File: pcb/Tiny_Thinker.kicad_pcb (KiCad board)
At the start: 4 copper layers, 65 x 63.1 mm, 42 parts, among them J2 PERIPHERALS, J3 ADC_TIM, J8 USB_C_Receptacle_USB2.0_16P, SW1 SW_Push, SW2 SW_SPDT, U1 STM32F446RET6, U2 AMS1117-3.3, Y1 16MHz

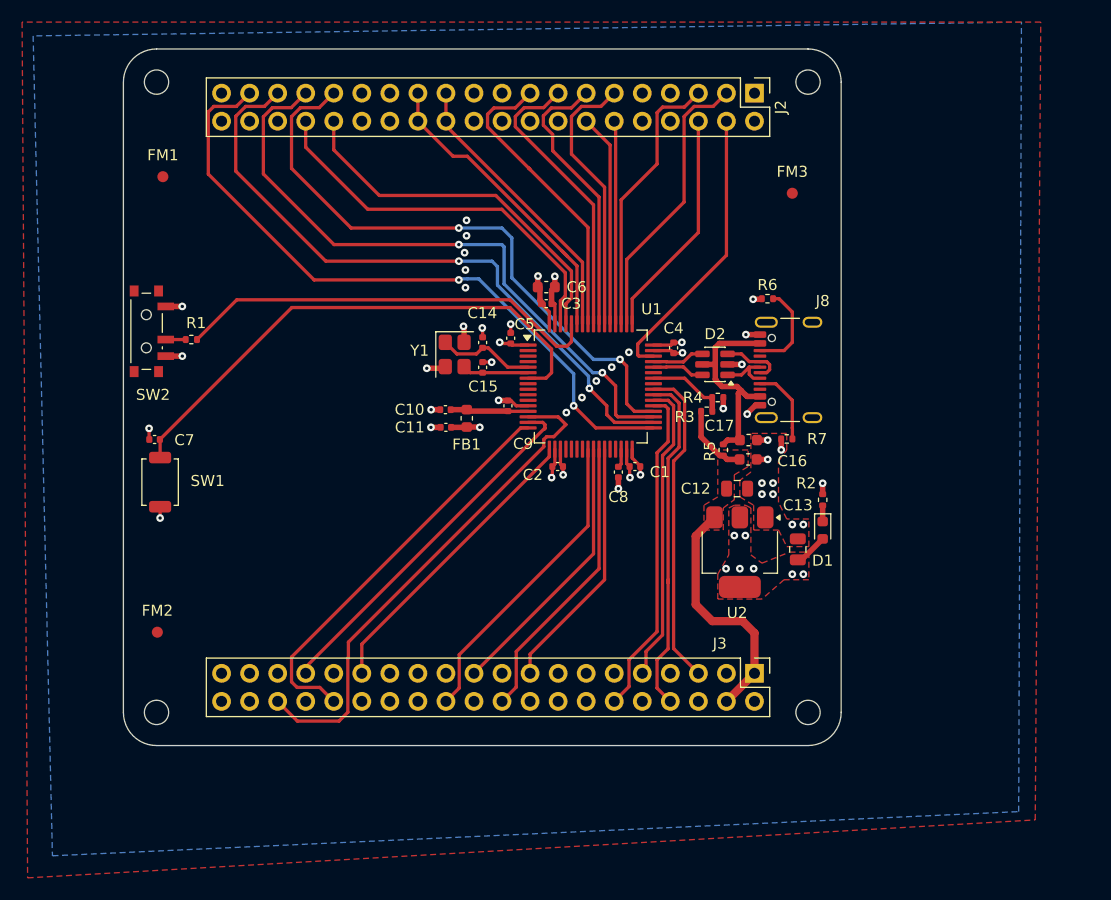
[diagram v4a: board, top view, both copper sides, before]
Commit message: finished adding vias to header pins (not stitching)
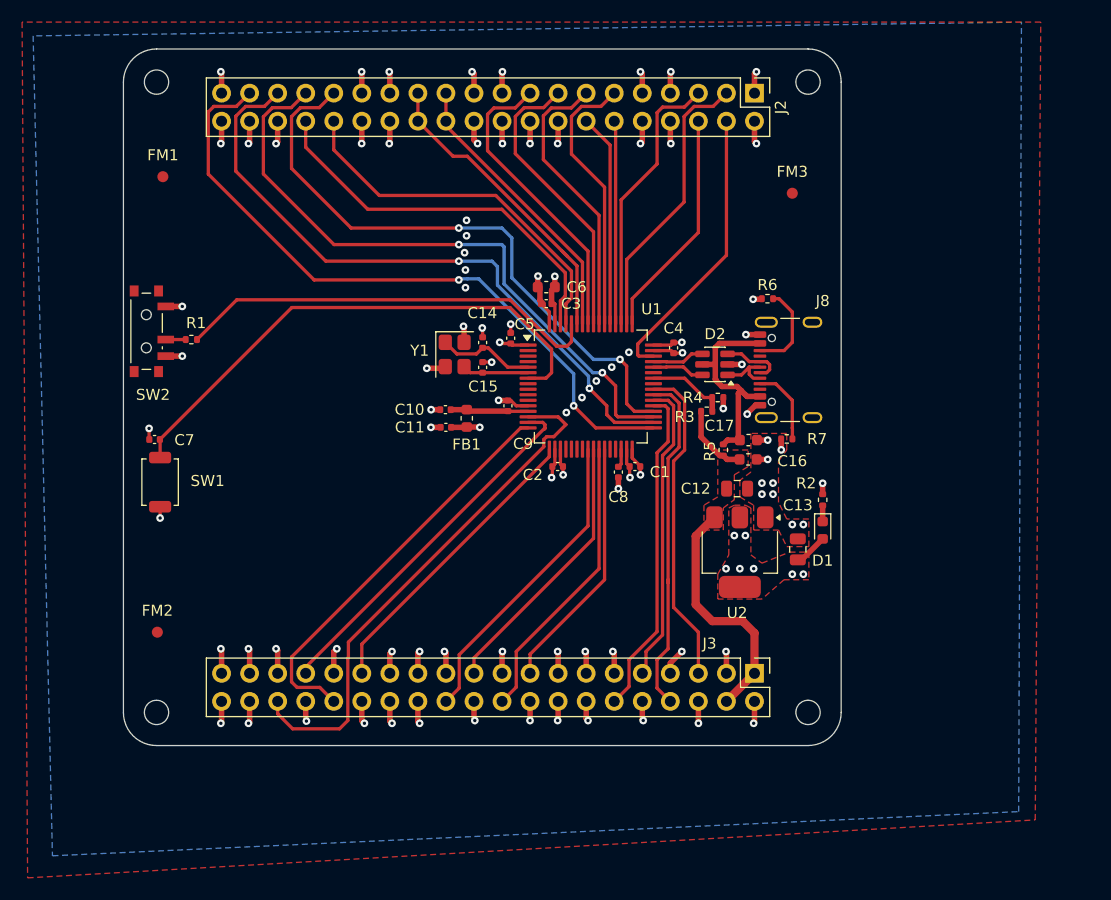
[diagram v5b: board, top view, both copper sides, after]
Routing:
- net GND: track 37.3 -> 97.9 mm, vias 41 -> 71
- net +3.3V: track 22.6 -> 54.9 mm, vias 14 -> 30
- net /TIM2_CH1: track 45.8 -> 47.4 mm

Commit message: started adding stitching vias
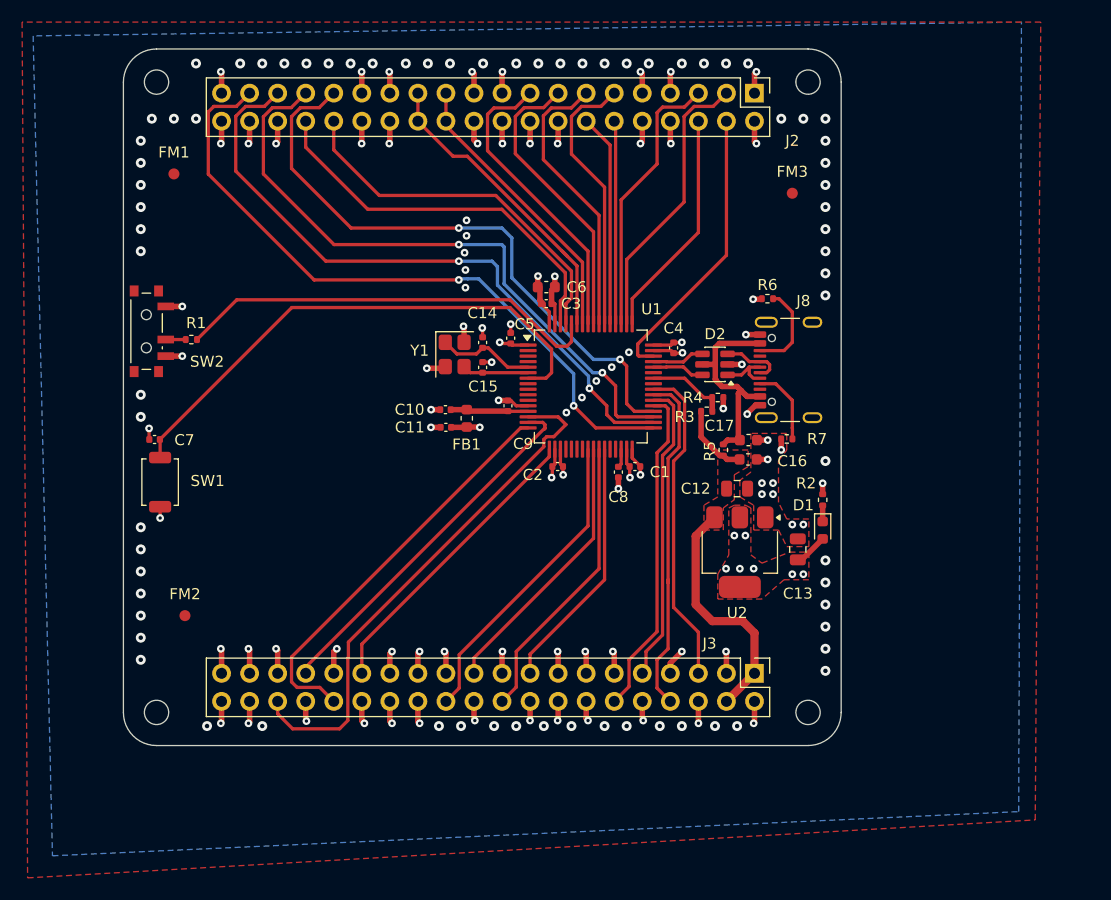
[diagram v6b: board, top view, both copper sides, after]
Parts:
- moved FM2 2.92 mm to (100.0, 122.0)
- moved FM1 1.03 mm to (99.0, 82.0)
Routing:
- net GND: vias 71 -> 144

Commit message: added logo
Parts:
- added G***: LOGO, LOGO, F.Cu at (112.0, 118.0)
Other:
- board text added: "Polar Robotics"
- board text added: "Tiny Thinker"
- board text added: "v1.0"

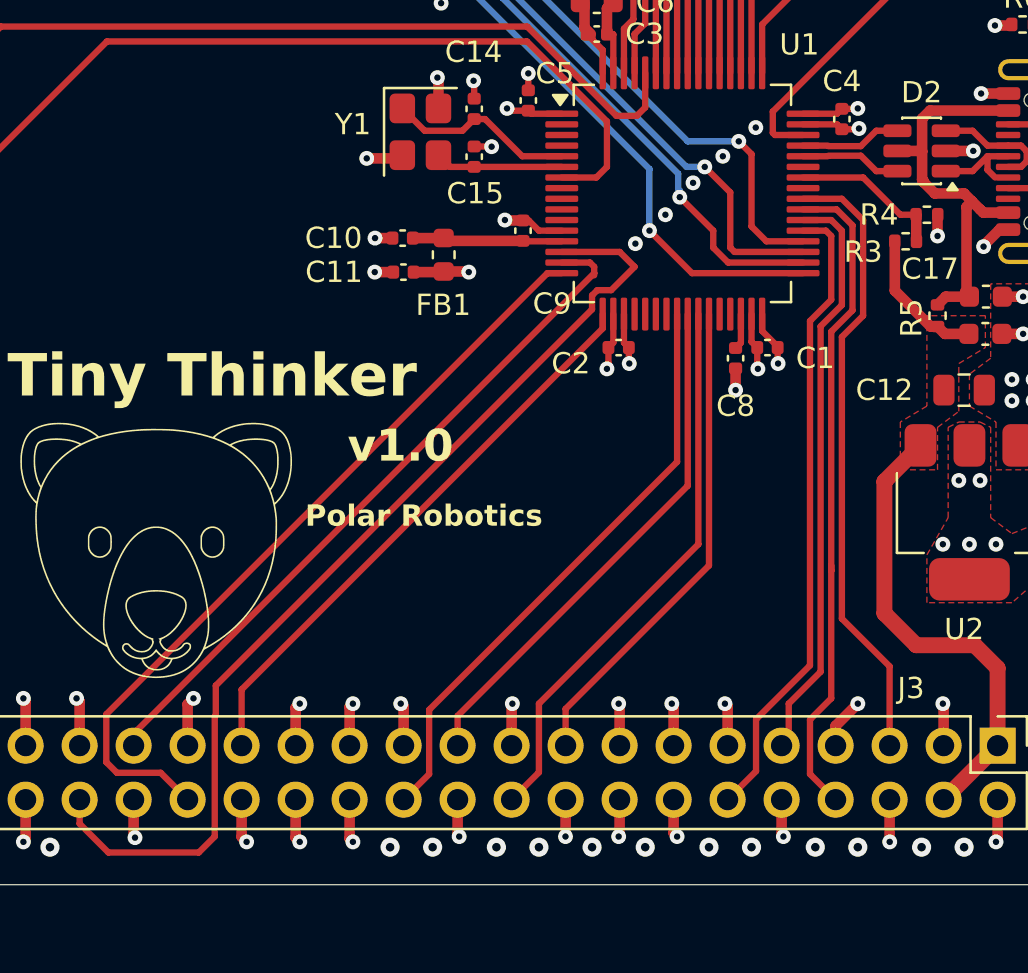
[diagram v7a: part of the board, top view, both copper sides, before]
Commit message: updated bom / added JLC part #
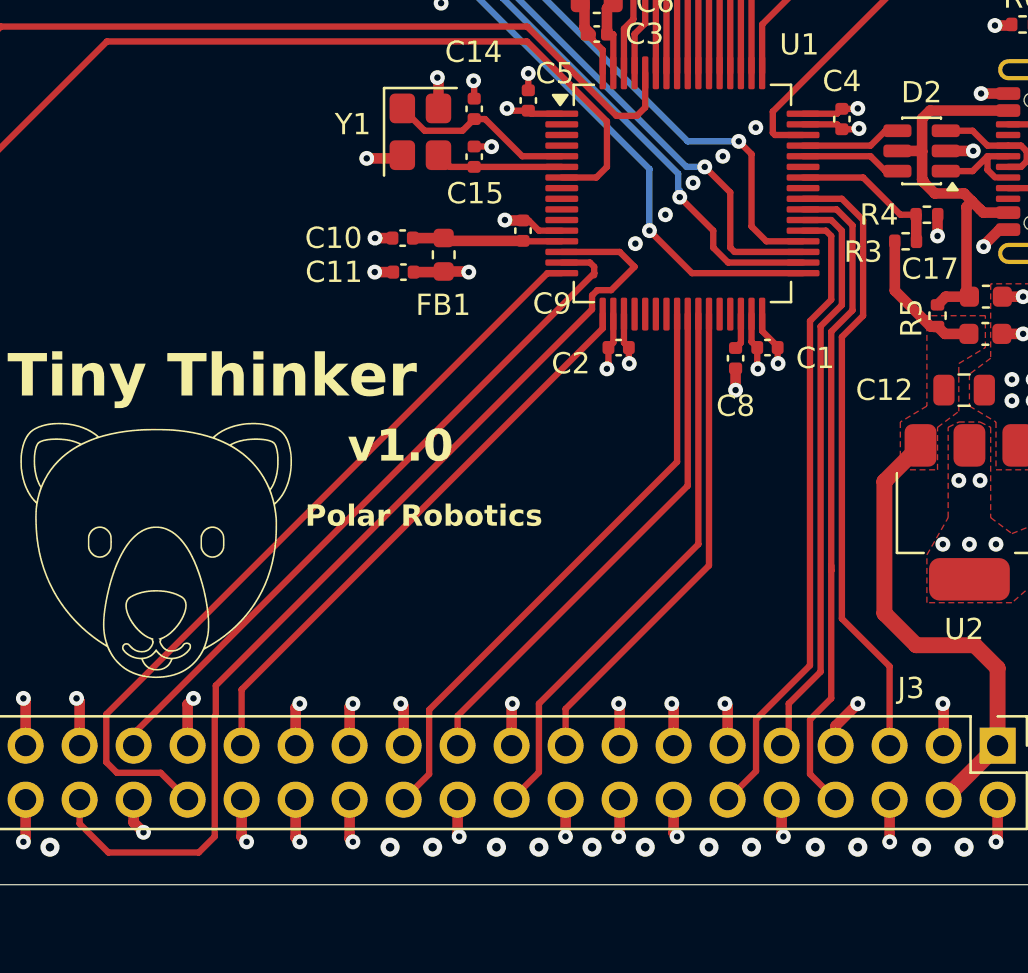
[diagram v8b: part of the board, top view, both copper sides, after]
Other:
- rule pad_to_mask_clearance: 0.1 -> 0
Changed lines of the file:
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@@
 			(dielectric_constraints no)
 		)
-		(pad_to_mask_clearance 0.1)
-		(solder_mask_min_width 0.1)
+		(pad_to_mask_clearance 0)
 		(allow_soldermask_bridges_in_footprints no)
 		(tenting front back)
@@
 	)
 	(segment
-		(start 110.935 129.765)
-		(end 110.935 131.485)
-		(width 0.5)
-		(layer "F.Cu")
-		(net 1)
-	)
-	(segment
 		(start 113.475 125.275)
 		(end 113.75 125)
@@
 	)
 	(segment
-		(start 110.935 131.485)
-		(end 111 131.55)
-		(width 0.5)
-		(layer "F.Cu")
-		(net 1)
-	)
-	(segment
 		(start 133.495 92.25)
 		(end 133.495 91.275)
@@
 	)
 	(segment
+		(start 110.935 130.835)
+		(end 110.935 129.765)
+		(width 0.5)
+		(layer "F.Cu")
+		(net 1)
+	)
+	(segment
 		(start 138.875 125.375)
 		(end 138.75 125.25)
@@
 	)
 	(segment
+		(start 111.4 131.3)
+		(end 110.935 130.835)
+		(width 0.5)
+		(layer "F.Cu")
+		(net 1)
+	)
+	(segment
 		(start 128.715 127.225)
 		(end 128.715 125.285)
@@
 	)
 	(via
-		(at 111 131.55)
+		(at 111.4 131.3)
 		(size 0.7)
 		(drill 0.3)
@@
 	)
 	(segment
+		(start 142.425 99)
+		(end 145.6 99)
+		(width 0.3)
+		(layer "F.Cu")
+		(net 8)
+	)
+	(segment
 		(start 152.07 99)
 		(end 152.678824 99)
@@
 	)
 	(segment
+		(start 145.6 99)
+		(end 146.3 98.3)
+		(width 0.3)
+		(layer "F.Cu")
+		(net 8)
+	)
+	(segment
 		(start 149.1375 98.3)
 		(end 150.399943 98.3)
@@
 	)
 	(segment
-		(start 152.946 99.267176)
-		(end 152.946 99.732824)
+		(start 146.3 98.3)
+		(end 146.8625 98.3)
 		(width 0.3)
 		(layer "F.Cu")
@@
 	)
 	(segment
-		(start 150.399943 98.3)
-		(end 151.101 99.001057)
+		(start 152.946 99.267176)
+		(end 152.946 99.732824)
 		(width 0.3)
 		(layer "F.Cu")
@@
 	)
 	(segment
-		(start 145.868749 98.3)
-		(end 146.8625 98.3)
+		(start 150.399943 98.3)
+		(end 151.101 99.001057)
 		(width 0.3)
 		(layer "F.Cu")
@@
 	)
 	(segment
-		(start 143.587501 99)
-		(end 143.612501 99.025)
-		(width 0.2)
-		(layer "F.Cu")
-		(net 8)
-	)
-	(segment
-		(start 143.612501 99.025)
-		(end 145.143749 99.025)
-		(width 0.3)
-		(layer "F.Cu")
-		(net 8)
-	)
-	(segment
-		(start 145.143749 99.025)
-		(end 145.868749 98.3)
-		(width 0.3)
-		(layer "F.Cu")
-		(net 8)
-	)
-	(segment
-		(start 142.425 99)
-		(end 143.587501 99)
-		(width 0.3)
-		(layer "F.Cu")
-		(net 8)
-	)
-	(segment
 		(start 152.678824 100)
 		(end 152.07 100)
@@
 	)
 	(segment
-		(start 143.587501 99.5)
-		(end 143.612501 99.475)
-		(width 0.2)
+		(start 151.101 100.139824)
+		(end 151.461176 100.5)
+		(width 0.3)
 		(layer "F.Cu")
 		(net 9)
 	)
 	(segment
-		(start 151.101 100.139824)
-		(end 151.461176 100.5)
+		(start 145.6 99.5)
+		(end 146.3 100.2)
 		(width 0.3)
 		(layer "F.Cu")
@@
 	)
 	(segment
-		(start 143.612501 99.475)
-		(end 145.143749 99.475)
-		(width 0.3)
-		(layer "F.Cu")
-		(net 9)
-	)
-	(segment
 		(start 151.102057 99.5)
 		(end 152.07 99.5)
@@
 	)
 	(segment
-		(start 145.868749 100.2)
+		(start 146.3 100.2)
 		(end 146.8625 100.2)
 		(width 0.3)
@@
 	)
 	(segment
-		(start 149.1375 100.2)
-		(end 150.399943 100.2)
+		(start 142.425 99.5)
+		(end 145.6 99.5)
 		(width 0.3)
 		(layer "F.Cu")
@@
 	)
 	(segment
-		(start 142.425 99.5)
-		(end 143.587501 99.5)
+		(start 149.1375 100.2)
+		(end 150.399943 100.2)
 		(width 0.3)
 		(layer "F.Cu")
@@
 	)
 	(segment
-		(start 145.143749 99.475)
-		(end 145.868749 100.2)
-		(width 0.3)
-		(layer "F.Cu")
-		(net 9)
-	)
-	(segment
 		(start 140.5 95.575)
 		(end 140.5 93.3)
@@
 	)
 	(segment
-		(start 134.6 89.432959)
-		(end 134.183521 89.016479)
+		(start 135.5 95.575)
+		(end 135.5 90.332958)
 		(width 0.3)
 		(layer "F.Cu")
@@
 	)
 	(segment
-		(start 135.5 90.332958)
+		(start 134.6 89.432959)
 		(end 134.183521 89.016479)
 		(width 0.3)
@@
 	)
 	(segment
-		(start 135.5 95.575)
-		(end 135.5 90.332958)
+		(start 135.5 90.332958)
+		(end 134.183521 89.016479)
 		(width 0.3)
 		(layer "F.Cu")
